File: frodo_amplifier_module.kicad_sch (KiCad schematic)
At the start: 19 parts, among them IC1 INA826AID, IC2 AS321KTR-G1, J1 Conn_01x01_Socket, J2 Conn_01x01_Socket, J3 Conn_01x01_Socket, J4 Conn_01x01_Socket, J5 Conn_01x01_Socket, J6 Conn_01x01_Socket, J7 Conn_01x01_Socket, J8 Conn_01x01_Socket

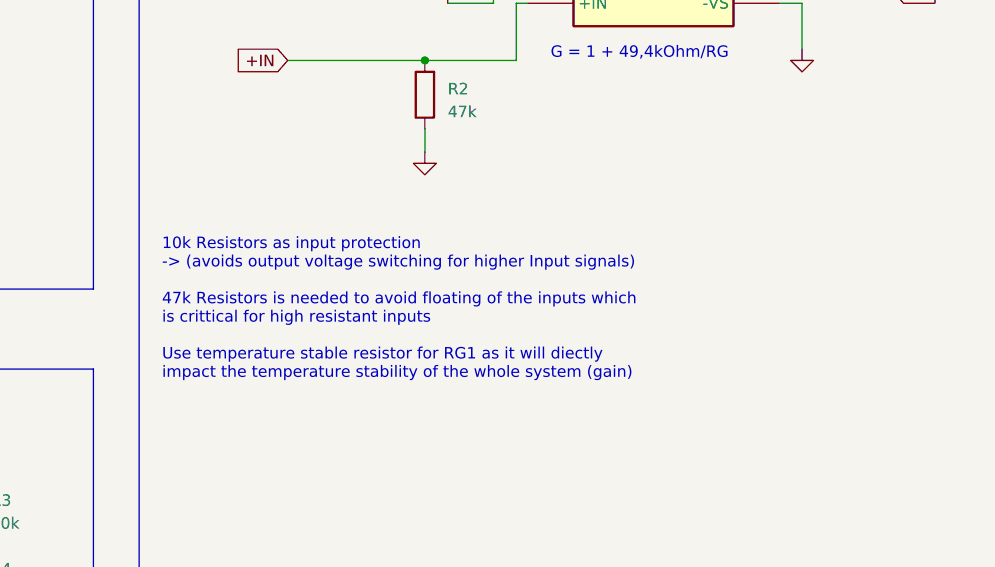
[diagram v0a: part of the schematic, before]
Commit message: changed folder layout, optimised gnd routing
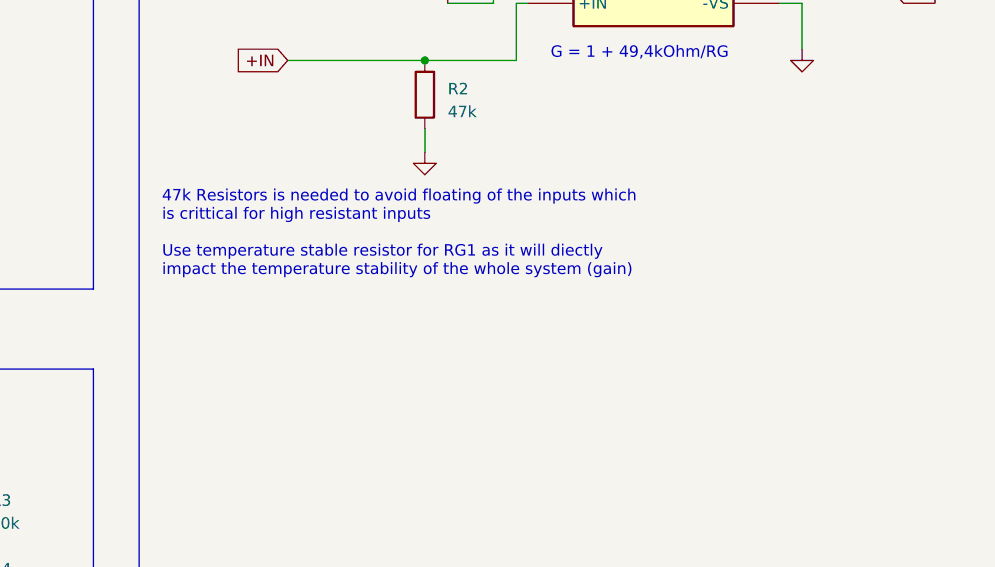
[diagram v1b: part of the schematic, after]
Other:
- note added: "47k Resistors is needed to avoid floating of the inputs which is crittical for high resistant inputs Use temperature stable resistor for RG1 as it will diectly impact the temperature stability of the whole system (gain)"
- note removed: "10k Resistors as input protection -> (avoids output voltage switching for higher Input signals) 47k Resistors is needed to avoid floating of the inputs which is crittical for high resistant inputs Use temperature stable resistor for RG1 as it will diectly impact the temperature stability of the whole system (gain)"
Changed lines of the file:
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@@
     (effects (font (size 2.5 2.5) (thickness 0.5) bold) (justify left bottom))
   )
-  (text "10k Resistors as input protection \n-> (avoids output voltage switching for higher Input signals)\n\n47k Resistors is needed to avoid floating of the inputs which\nis crittical for high resistant inputs\n\nUse temperature stable resistor for RG1 as it will diectly\nimpact the temperature stability of the whole system (gain)"
-    (at 139.7 109.22 0)
+  (text "47k Resistors is needed to avoid floating of the inputs which\nis crittical for high resistant inputs\n\nUse temperature stable resistor for RG1 as it will diectly\nimpact the temperature stability of the whole system (gain)"
+    (at 139.7 97.79 0)
     (effects (font (size 1.27 1.27)) (justify left bottom))
   )

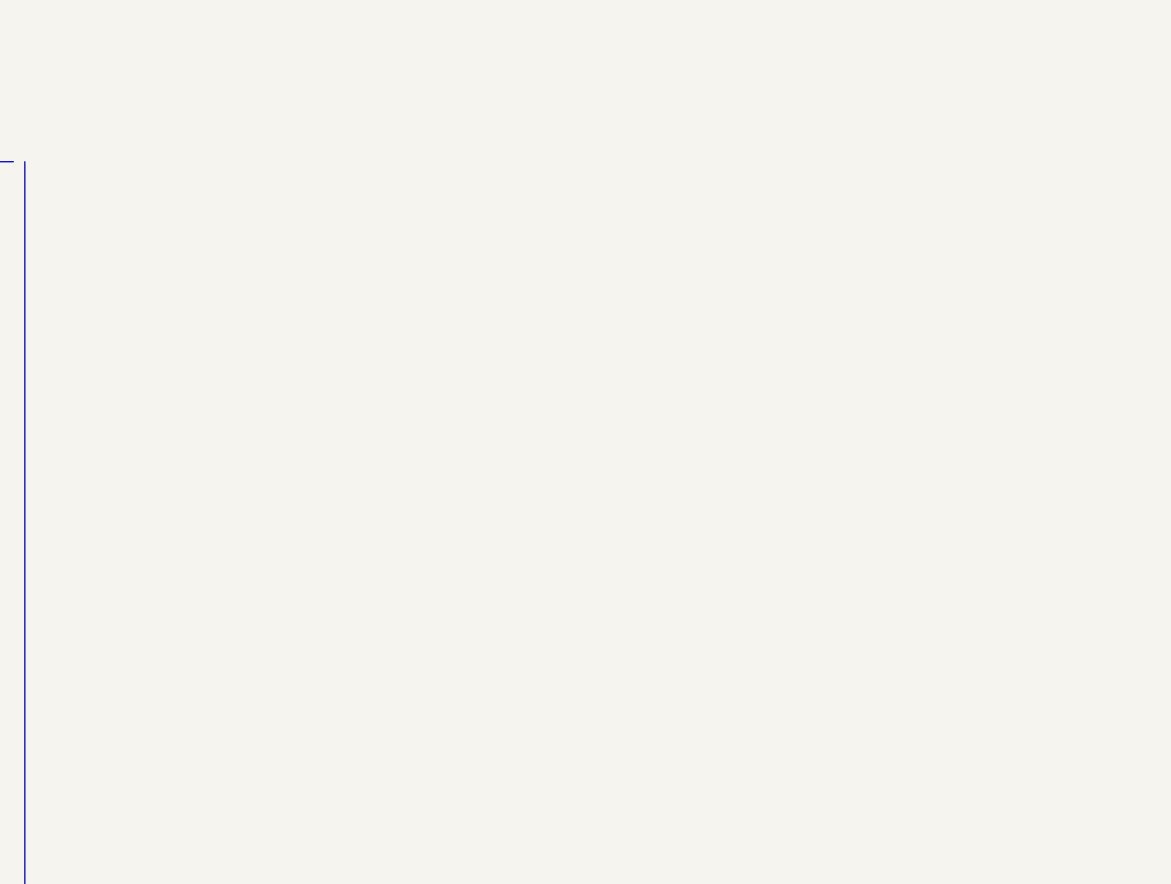
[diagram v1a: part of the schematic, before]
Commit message: started adding wika recomendations
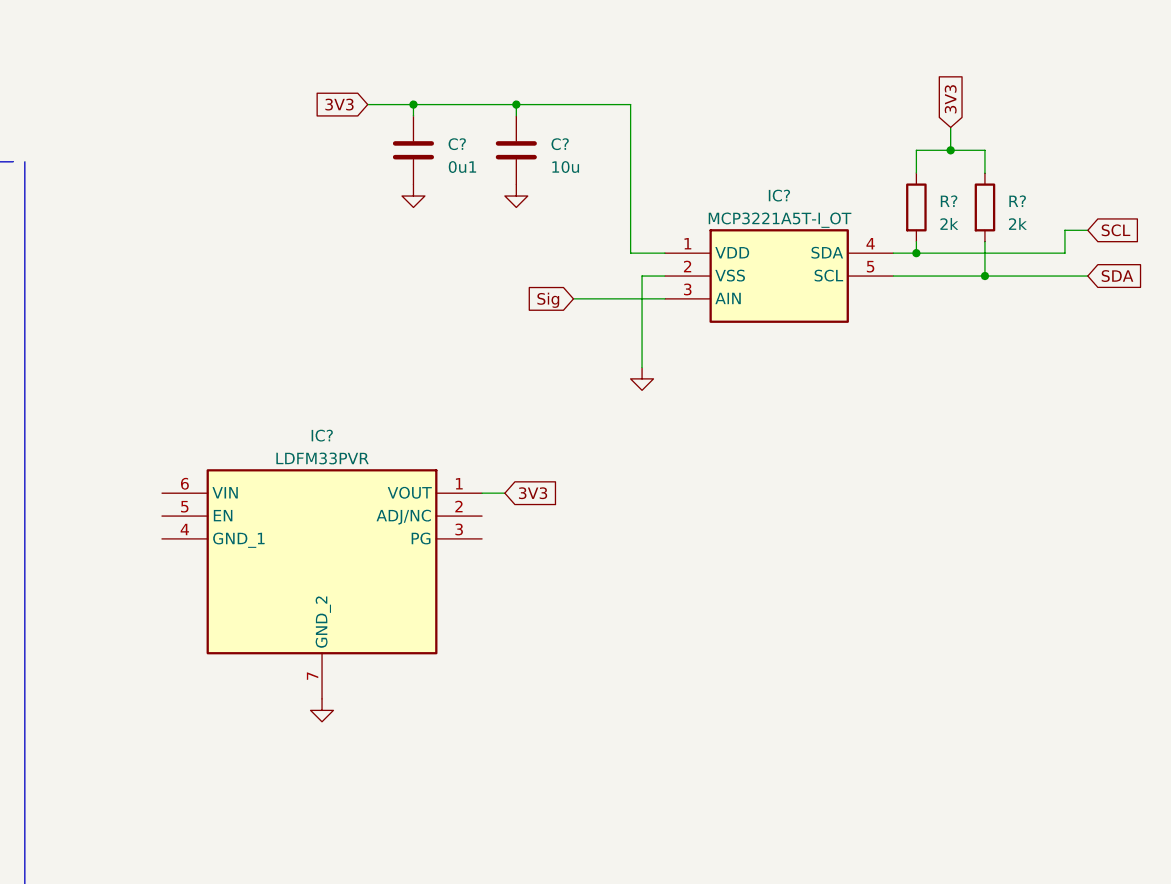
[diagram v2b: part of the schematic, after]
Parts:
- added C?: 0u1, symbol Device:C
- added C?: 10u, symbol Device:C
- added IC?: MCP3221A5T-I_OT, SOT95P280X145-5N, symbol MCP3221A5T-I_OT:MCP3221A5T-I_OT
- added IC?: LDFM33PVR, SON65P200X200X100-7N-D, symbol LDFM33PVR:LDFM33PVR
- added R? (x2): 2k, symbol Device:R
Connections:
- net GND: now also C?.2, C?.2, IC?.2 (VSS), IC?.7 (GND_2)
- new net 3V3: C?.1, C?.1, IC?.1 (VDD), IC?.1 (VOUT), R?.1, R?.1
- new net SCL: IC?.4 (SDA), R?.2
- new net SDA: IC?.5 (SCL), R?.2
- new net Sig: IC?.3 (AIN)

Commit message: continued working on v0.2
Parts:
- removed IC?: LDFM33PVR, SON65P200X200X100-7N-D, symbol LDFM33PVR:LDFM33PVR
- added C? (x2): 2n2, symbol Device:C
- added C? (x2): 1u, symbol Device:C
- added C?: 0u1, symbol Device:C
- added C?: 10n, symbol Device:C
- added FB?: 120R, Inductor_SMD:L_0603_1608Metric, symbol Device:FerriteBead
- added JP?: SolderJumper_3_Open, Jumper:SolderJumper-3_P1.3mm_Open_RoundedPad1.0x1.5mm_NumberLabels, symbol Jumper:SolderJumper_3_Open
- added U?: MIC5504-3.3YM5, Package_TO_SOT_SMD:SOT-23-5, symbol Regulator_Linear:MIC5504-3.3YM5
- R? (x2): value 2k -> 10k
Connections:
- net +IN: now also C?.1, C?.1
- net -IN: now also C?.1, C?.2
- net 3V3: now also C1.1, IC1.8 (+VS), IC2.5 (VCC), R3.2, C?.1, JP?.3 (B), U?.5 (VOUT)
- net GND: now also C?.2, C?.2, C?.2, C?.2, C?.2, FB?.2, U?.2 (GND); no longer J4.1 (Pin_1)
- net SCL: now also IC?.5 (SCL), J2.1 (Pin_1), R?.2; no longer IC?.4 (SDA), R?.2
- net SDA: now also IC?.4 (SDA), J3.1 (Pin_1), R?.2; no longer IC?.5 (SCL), R?.2
- net ref: no longer J3.1 (Pin_1)
- removed net VDD: C1.1, C2.1, FB1.2, IC1.8 (+VS), IC2.5 (VCC), J5.1 (Pin_1), R3.2
- net out renamed sig
- net sig: no longer J2.1 (Pin_1)
- new net: J5.1 (Pin_1), JP?.1 (A)
- new net: FB?.1, J4.1 (Pin_1)
- new net 5V: C2.1, C?.1, C?.1, FB1.2, JP?.2 (C), U?.1 (VIN), U?.3 (EN)
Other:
- note added: "5V from io board"
- note added: "FerriteBead for filtering noise on power lines"
- note added: "Input signal should be of low impedance. Use buffer to archive this! probably MCP6021 (maybe also a dual opamp -> also as reference)"
- note added: "Voltage Regulator"
- note added: "possibility to supply 5V (may be neccesarry for some sensors)"
- note added: "pullup resistors, typically: - 10 kΩ for 100 kHz - 2 kΩ for 400 kHz SCL clock speeds"
- note added: "this got a 2% accuracy, for more accuracy (1%) chose Texas Instruments: TLV74033PDBVR"
- note removed: "FerriteBead for filtering noise on power line"
- note removed: "Singlesupply 3V to 36V"
- moved on the sheet: C2, C?, FB1, IC2, IC?, J1, J3, J4, J5, J6, J7, J8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

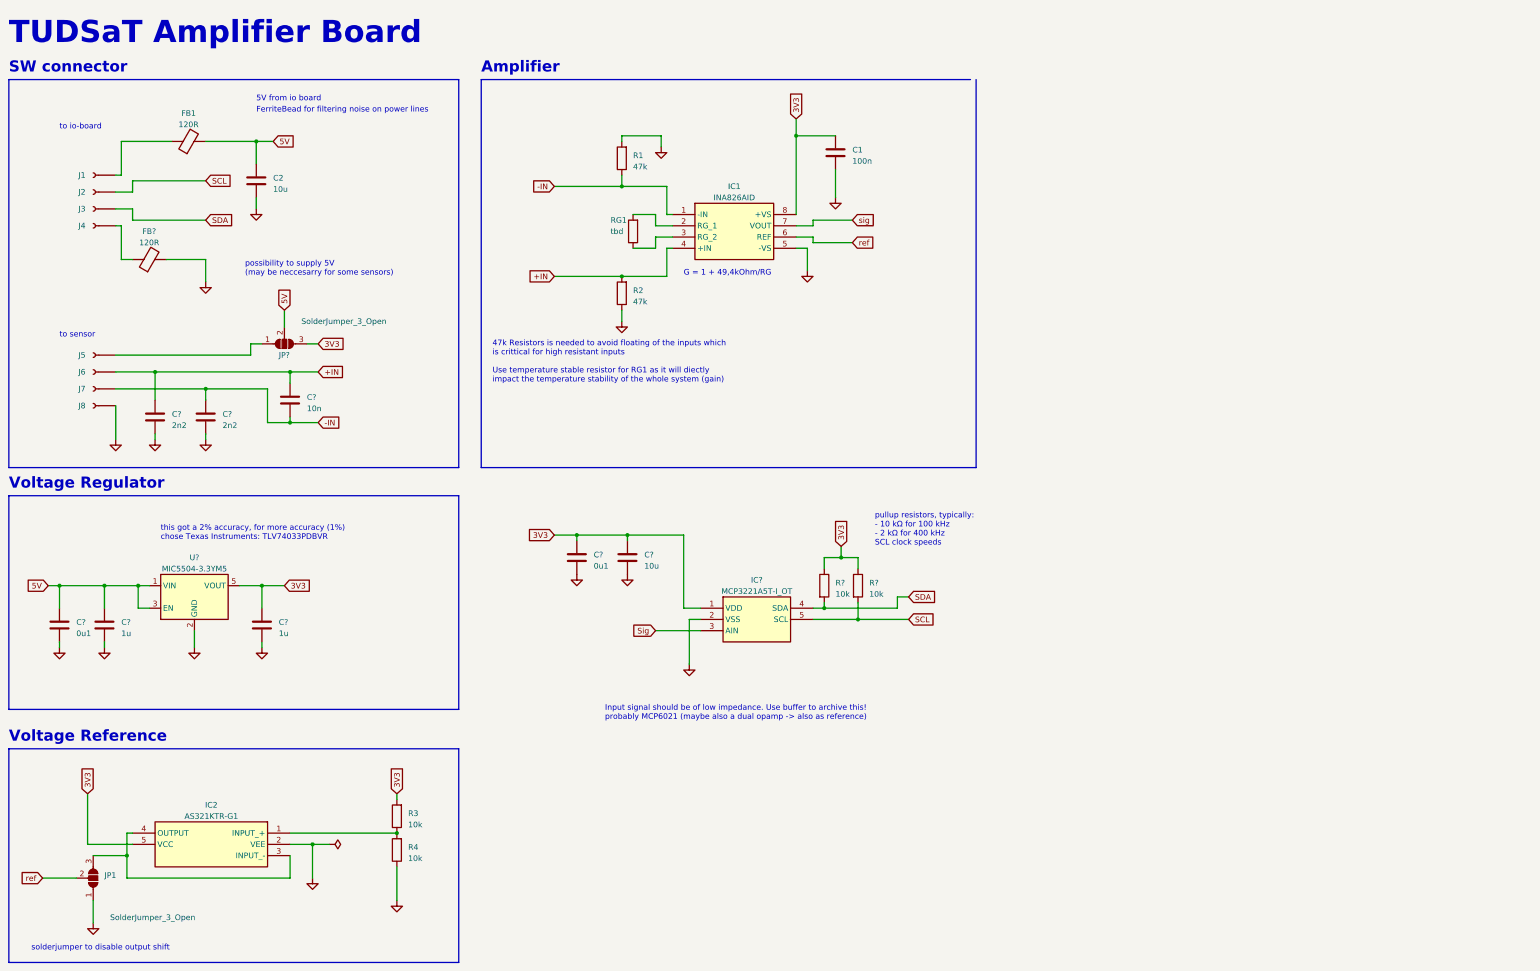
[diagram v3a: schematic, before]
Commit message: implemented wikas recomendations to scematic
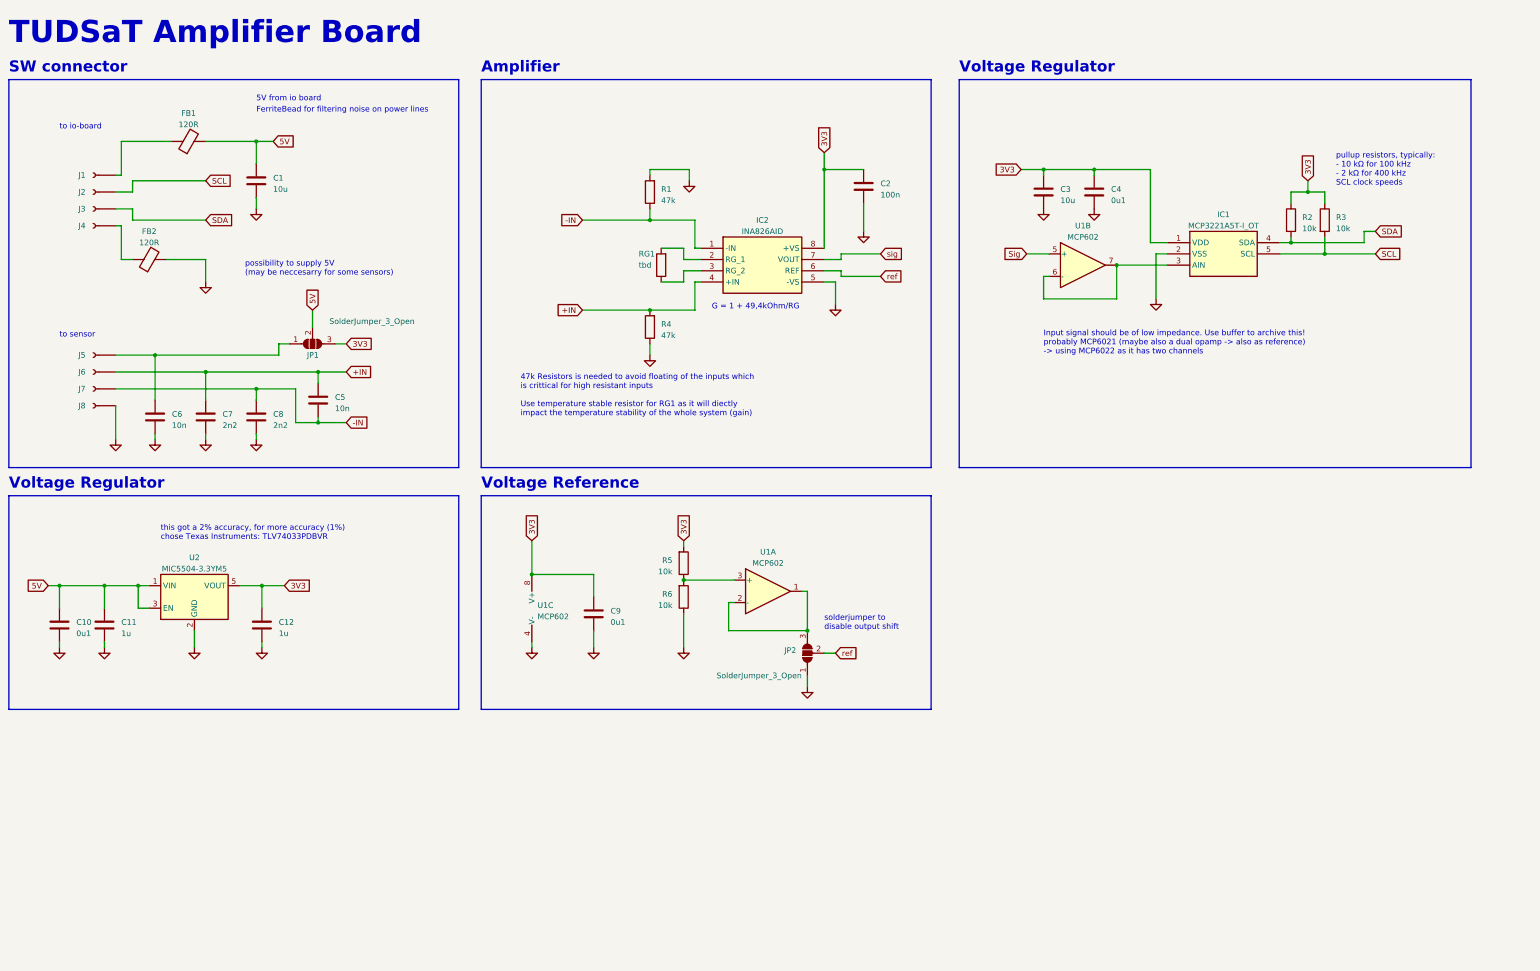
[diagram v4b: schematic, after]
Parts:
- removed IC2: AS321KTR-G1, Package_TO_SOT_SMD:SOT-23-5, symbol AS321KTR-G1:AS321KTR-G1
- removed JP1: SolderJumper_3_Open, Jumper:SolderJumper-3_P1.3mm_Open_RoundedPad1.0x1.5mm_NumberLabels, symbol Jumper:SolderJumper_3_Open
- removed R3, R4: 10k, Resistor_SMD:R_0402_1005Metric_Pad0.72x0.64mm_HandSolder, symbol Device:R
- added C6: 10n, Capacitor_SMD:C_0402_1005Metric, symbol Device:C
- added C9: 0u1, Capacitor_SMD:C_0402_1005Metric, symbol Device:C
- added JP2: SolderJumper_3_Open, Jumper:SolderJumper-3_P1.3mm_Open_RoundedPad1.0x1.5mm_NumberLabels, symbol Jumper:SolderJumper_3_Open
- added R5, R6: 10k, Resistor_SMD:R_0402_1005Metric_Pad0.72x0.64mm_HandSolder, symbol Device:R
- added U1: MCP602, Package_SO:SOIC-8-1EP_3.9x4.9mm_P1.27mm_EP2.29x3mm, symbol Amplifier_Operational:MCP602
- C10, C11, C12, C5, C7, C8: renamed from C?; footprint (none) -> Capacitor_SMD:C_0402_1005Metric
- C2: renamed from C1; footprint Capacitor_SMD:C_0402_1005Metric_Pad0.74x0.62mm_HandSolder -> Capacitor_SMD:C_0402_1005Metric
- C3: renamed from C?; value 0u1 -> 10u; footprint (none) -> Capacitor_SMD:C_0603_1608Metric
- C4: renamed from C?; value 10u -> 0u1; footprint (none) -> Capacitor_SMD:C_0402_1005Metric
- IC1: renamed from IC?; footprint SOT95P280X145-5N -> Package_TO_SOT_SMD:SOT-23-5
- R2, R3: renamed from R?; footprint (none) -> Resistor_SMD:R_0402_1005Metric
- gave numbers to parts that had none: 3
- renumbered C2 to C1, IC1 to IC2, R2 to R4
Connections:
- net 3V3: now also C9.1, R5.2, U1.8 (V+)
- net GND: now also C6.2, C9.2, JP2.1 (A), R6.1, U1.4 (V-)
- net Sig: now also U1.5 (+); no longer IC1.3 (AIN)
- net ref: now also JP2.2 (C)
- net at J5.1 (Pin_1), JP1.1 (A): now also C6.1
- new net: R5.1, R6.2, U1.3 (+)
- new net: JP2.3 (B), U1.1, U1.2 (-)
- new net: IC1.3 (AIN), U1.6 (-), U1.7
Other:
- note added: "Input signal should be of low impedance. Use buffer to archive this! probably MCP6021 (maybe also a dual opamp -> also as reference) -> using MCP6022 as it has two channels"
- note removed: "Input signal should be of low impedance. Use buffer to archive this! probably MCP6021 (maybe also a dual opamp -> also as reference)"
- moved on the sheet: C2, C3, C4, C5, C7, C8, IC1, IC2, JP1, R1, R2, R3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
